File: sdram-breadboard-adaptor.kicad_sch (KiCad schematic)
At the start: 18 parts, among them J0 Conn_01x40, J1 Conn_01x40, U0 LY62W10248ML-55LLI, U1 LY62W10248ML-55LLI, U2 LY62W10248ML-55LLI, U3 LY62W10248ML-55LLI, U4 LY62W10248ML-55LLI, U5 LY62W10248ML-55LLI, U6 LY62W10248ML-55LLI, U7 LY62W10248ML-55LLI

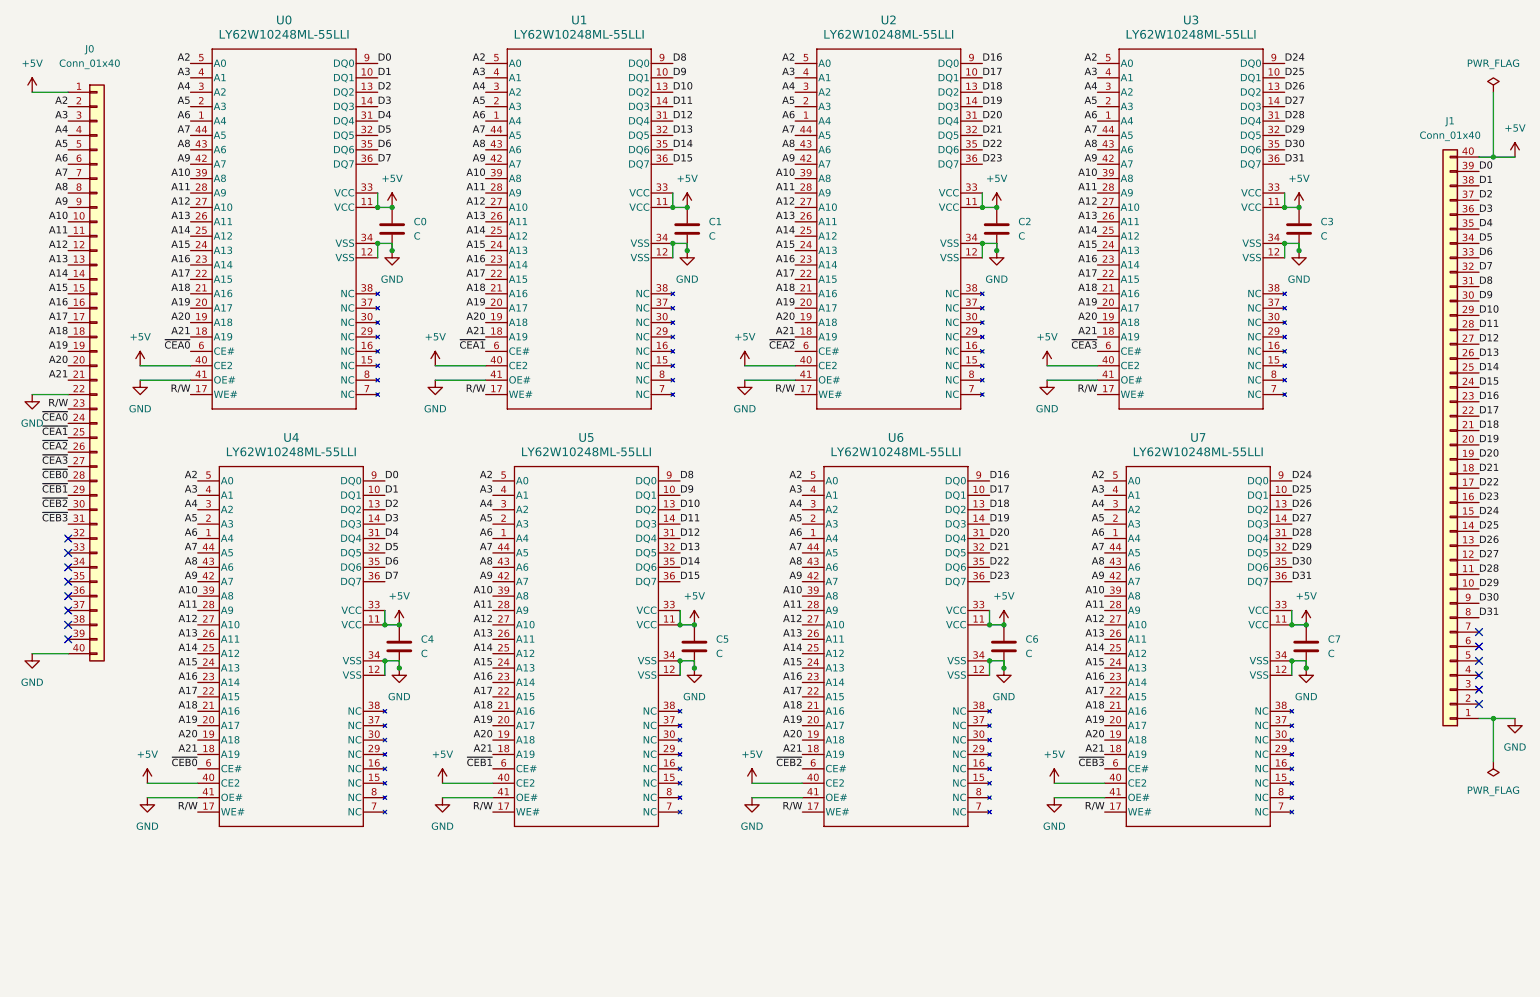
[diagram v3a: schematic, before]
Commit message: add bypass caps
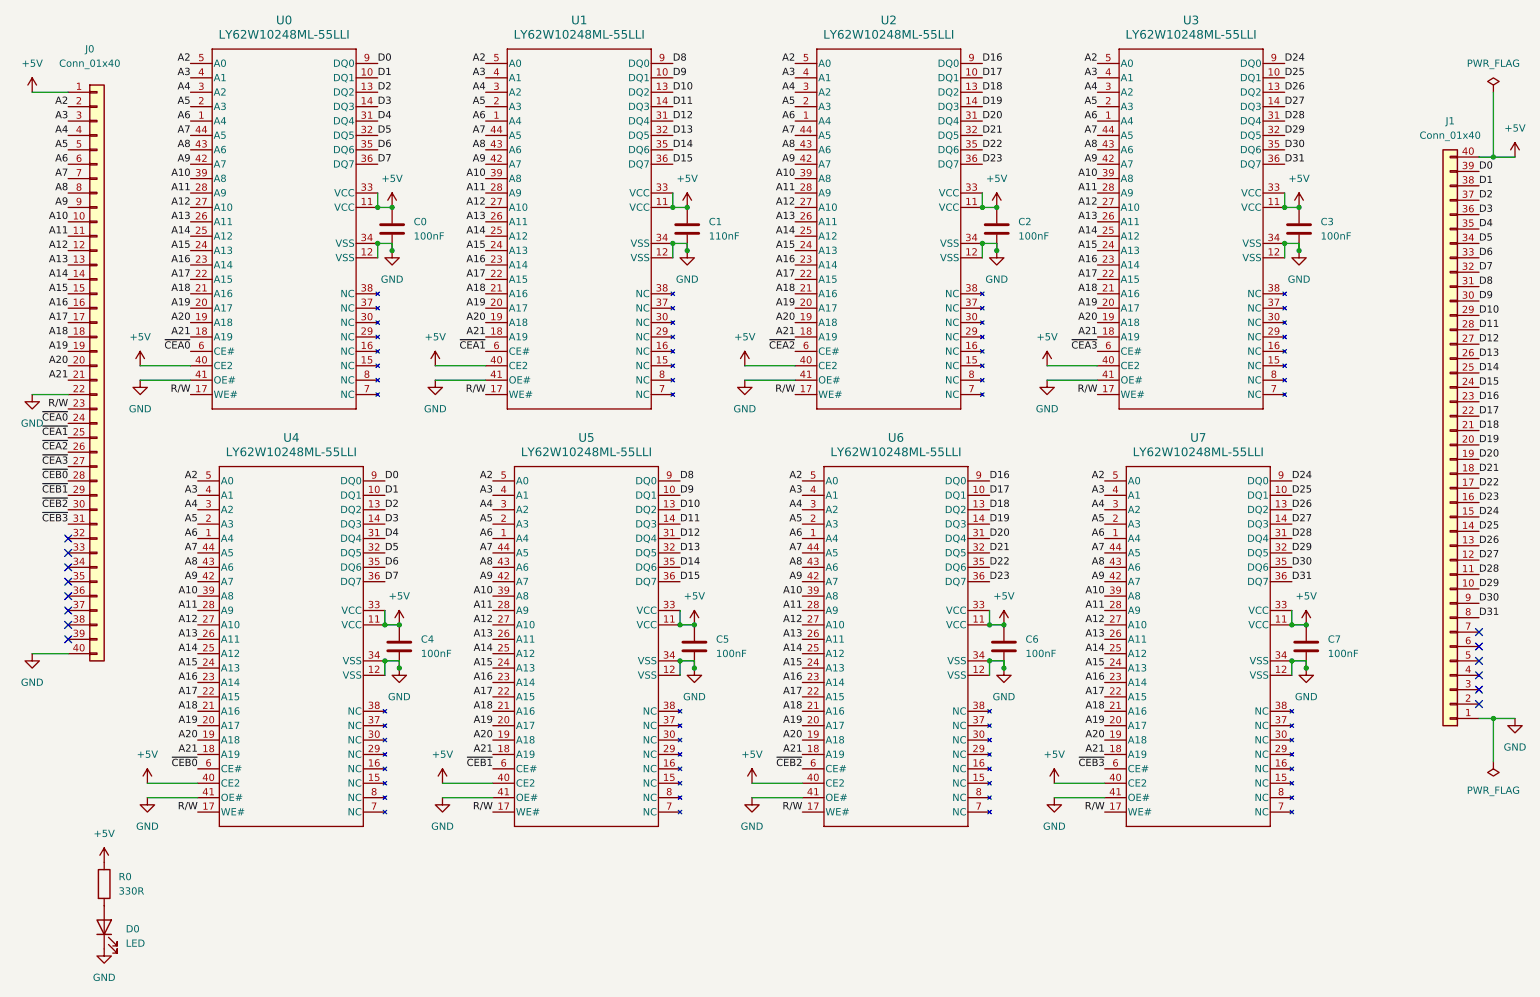
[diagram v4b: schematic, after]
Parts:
- added D0: LED, LED_SMD:LED_0805_2012Metric_Pad1.15x1.40mm_HandSolder, symbol Device:LED
- added R0: 330R, Resistor_SMD:R_0805_2012Metric_Pad1.20x1.40mm_HandSolder, symbol Device:R
- C0, C2, C3, C4, C5, C6, C7: value C -> 100nF; footprint (none) -> Capacitor_SMD:C_0805_2012Metric_Pad1.18x1.45mm_HandSolder
- C1: value C -> 110nF; footprint (none) -> Capacitor_SMD:C_0805_2012Metric_Pad1.18x1.45mm_HandSolder
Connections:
- net +5V: now also R0.1
- net GND: now also D0.1 (K)
- new net: D0.2 (A), R0.2
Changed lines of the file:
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@@
       (effects (font (size 1.27 1.27)) (justify left))
     )
-    (property "Value" "C" (at 135.89 128.27 0)
+    (property "Value" "100nF" (at 135.89 128.27 0)
       (effects (font (size 1.27 1.27)) (justify left))
     )
-    (property "Footprint" "" (at 133.0452 130.81 0)
+    (property "Footprint" "Capacitor_SMD:C_0805_2012Metric_Pad1.18x1.45mm_HandSolder" (at 133.0452 130.81 0)
       (effects (font (size 1.27 1.27)) hide)
     )
@@
       (effects (font (size 1.27 1.27)) (justify left))
     )
-    (property "Value" "C" (at 134.62 54.61 0)
+    (property "Value" "110nF" (at 134.62 54.61 0)
       (effects (font (size 1.27 1.27)) (justify left))
     )
-    (property "Footprint" "" (at 131.7752 57.15 0)
+    (property "Footprint" "Capacitor_SMD:C_0805_2012Metric_Pad1.18x1.45mm_HandSolder" (at 131.7752 57.15 0)
       (effects (font (size 1.27 1.27)) hide)
     )
@@
         (path "/60b81836-8f7a-4164-b458-6cd35546367f"
           (reference "C1") (unit 1)
+        )
+      )
+    )
+  )
+  (symbol (lib_id "power:GND") (at 27.94 180.34 0) (unit 1)
+    (in_bom yes) (on_board yes) (dnp no) (fields_autoplaced)
+    (property "Reference" "#PWR038" (at 27.94 186.69 0)
+      (effects (font (size 1.27 1.27)) hide)
+    )
+    (property "Value" "GND" (at 27.94 185.42 0)
+      (effects (font (size 1.27 1.27)))
+    )
+    (property "Footprint" "" (at 27.94 180.34 0)
+      (effects (font (size 1.27 1.27)) hide)
+    )
+    (property "Datasheet" "" (at 27.94 180.34 0)
+      (effects (font (size 1.27 1.27)) hide)
+    )
+    (pin "1")
+    (instances
+      (project "sdram-breadboard-adaptor"
+        (path "/60b81836-8f7a-4164-b458-6cd35546367f"
+          (reference "#PWR038") (unit 1)
         )
       )
@@
     )
   )
+  (symbol (lib_id "power:+5V") (at 27.94 165.1 0) (unit 1)
+    (in_bom yes) (on_board yes) (dnp no) (fields_autoplaced)
+    (property "Reference" "#PWR037" (at 27.94 168.91 0)
+      (effects (font (size 1.27 1.27)) hide)
+    )
+    (property "Value" "+5V" (at 27.94 160.02 0)
+      (effects (font (size 1.27 1.27)))
+    )
+    (property "Footprint" "" (at 27.94 165.1 0)
+      (effects (font (size 1.27 1.27)) hide)
+    )
+    (property "Datasheet" "" (at 27.94 165.1 0)
+      (effects (font (size 1.27 1.27)) hide)
+    )
+    (pin "1")
+    (instances
+      (project "sdram-breadboard-adaptor"
+        (path "/60b81836-8f7a-4164-b458-6cd35546367f"
+          (reference "#PWR037") (unit 1)
+        )
+      )
+    )
+  )
   (symbol (lib_id "LYONTEK:LY62W10248ML-55LLI") (at 92.71 102.87 0) (unit 1)
     (in_bom yes) (on_board yes) (dnp no) (fields_autoplaced)
@@
       (effects (font (size 1.27 1.27)) (justify left))
     )
-    (property "Value" "C" (at 243.84 128.27 0)
+    (property "Value" "100nF" (at 243.84 128.27 0)
       (effects (font (size 1.27 1.27)) (justify left))
     )
-    (property "Footprint" "" (at 240.9952 130.81 0)
+    (property "Footprint" "Capacitor_SMD:C_0805_2012Metric_Pad1.18x1.45mm_HandSolder" (at 240.9952 130.81 0)
       (effects (font (size 1.27 1.27)) hide)
     )
@@
       (effects (font (size 1.27 1.27)) (justify left))
     )
-    (property "Value" "C" (at 82.55 54.61 0)
+    (property "Value" "100nF" (at 82.55 54.61 0)
       (effects (font (size 1.27 1.27)) (justify left))
     )
-    (property "Footprint" "" (at 79.7052 57.15 0)
+    (property "Footprint" "Capacitor_SMD:C_0805_2012Metric_Pad1.18x1.45mm_HandSolder" (at 79.7052 57.15 0)
       (effects (font (size 1.27 1.27)) hide)
     )
@@
     )
   )
+  (symbol (lib_id "Device:LED") (at 27.94 176.53 90) (unit 1)
+    (in_bom yes) (on_board yes) (dnp no) (fields_autoplaced)
+    (property "Reference" "D0" (at 31.75 176.8475 90)
+      (effects (font (size 1.27 1.27)) (justify right))
+    )
+    (property "Value" "LED" (at 31.75 179.3875 90)
+      (effects (font (size 1.27 1.27)) (justify right))
+    )
+    (property "Footprint" "LED_SMD:LED_0805_2012Metric_Pad1.15x1.40mm_HandSolder" (at 27.94 176.53 0)
+      (effects (font (size 1.27 1.27)) hide)
+    )
+    (property "Datasheet" "~" (at 27.94 176.53 0)
+      (effects (font (size 1.27 1.27)) hide)
+    )
+    (pin "1")
+    (pin "2")
+    (instances
+      (project "sdram-breadboard-adaptor"
+        (path "/60b81836-8f7a-4164-b458-6cd35546367f"
+          (reference "D0") (unit 1)
+        )
+      )
+    )
+  )
   (symbol (lib_id "power:GND") (at 185.42 57.15 0) (unit 1)
     (in_bom yes) (on_board yes) (dnp no) (fields_autoplaced)
@@
         (path "/60b81836-8f7a-4164-b458-6cd35546367f"
           (reference "#PWR023") (unit 1)
+        )
+      )
+    )
+  )
+  (symbol (lib_id "Device:R") (at 27.94 168.91 0) (unit 1)
+    (in_bom yes) (on_board yes) (dnp no) (fields_autoplaced)
+    (property "Reference" "R0" (at 30.48 167.64 0)
+      (effects (font (size 1.27 1.27)) (justify left))
+    )
+    (property "Value" "330R" (at 30.48 170.18 0)
+      (effects (font (size 1.27 1.27)) (justify left))
+    )
+    (property "Footprint" "Resistor_SMD:R_0805_2012Metric_Pad1.20x1.40mm_HandSolder" (at 26.162 168.91 90)
+      (effects (font (size 1.27 1.27)) hide)
+    )
+    (property "Datasheet" "~" (at 27.94 168.91 0)
+      (effects (font (size 1.27 1.27)) hide)
+    )
+    (pin "1")
+    (pin "2")
+    (instances
+      (project "sdram-breadboard-adaptor"
+        (path "/60b81836-8f7a-4164-b458-6cd35546367f"
+          (reference "R0") (unit 1)
         )
       )
@@
       (effects (font (size 1.27 1.27)) (justify left))
     )
-    (property "Value" "C" (at 190.5 128.27 0)
+    (property "Value" "100nF" (at 190.5 128.27 0)
       (effects (font (size 1.27 1.27)) (justify left))
     )
-    (property "Footprint" "" (at 187.6552 130.81 0)
+    (property "Footprint" "Capacitor_SMD:C_0805_2012Metric_Pad1.18x1.45mm_HandSolder" (at 187.6552 130.81 0)
       (effects (font (size 1.27 1.27)) hide)
     )
@@
       (effects (font (size 1.27 1.27)) (justify left))
     )
-    (property "Value" "C" (at 242.57 54.61 0)
+    (property "Value" "100nF" (at 242.57 54.61 0)
       (effects (font (size 1.27 1.27)) (justify left))
     )
-    (property "Footprint" "" (at 239.7252 57.15 0)
+    (property "Footprint" "Capacitor_SMD:C_0805_2012Metric_Pad1.18x1.45mm_HandSolder" (at 239.7252 57.15 0)
       (effects (font (size 1.27 1.27)) hide)
     )
@@
       (effects (font (size 1.27 1.27)) (justify left))
     )
-    (property "Value" "C" (at 83.82 128.27 0)
+    (property "Value" "100nF" (at 83.82 128.27 0)
       (effects (font (size 1.27 1.27)) (justify left))
     )
-    (property "Footprint" "" (at 80.9752 130.81 0)
+    (property "Footprint" "Capacitor_SMD:C_0805_2012Metric_Pad1.18x1.45mm_HandSolder" (at 80.9752 130.81 0)
       (effects (font (size 1.27 1.27)) hide)
     )
@@
       (effects (font (size 1.27 1.27)) (justify left))
     )
-    (property "Value" "C" (at 189.23 54.61 0)
+    (property "Value" "100nF" (at 189.23 54.61 0)
       (effects (font (size 1.27 1.27)) (justify left))
     )
-    (property "Footprint" "" (at 186.3852 57.15 0)
-      (effects (font (size 1.27 1.27)) hide)
-    )
+    (property "Footprint" "Capacitor_SMD:C_0805_2012Metric_Pad1.18x1.45mm_HandSolder" (at 186.3852 57.15 0)
+      (effects (font (size 1.27 1.27)) hide)
+    )
